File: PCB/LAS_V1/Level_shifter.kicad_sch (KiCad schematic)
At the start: 6 parts, among them Q4 AO3400A, Q5 AO3400A

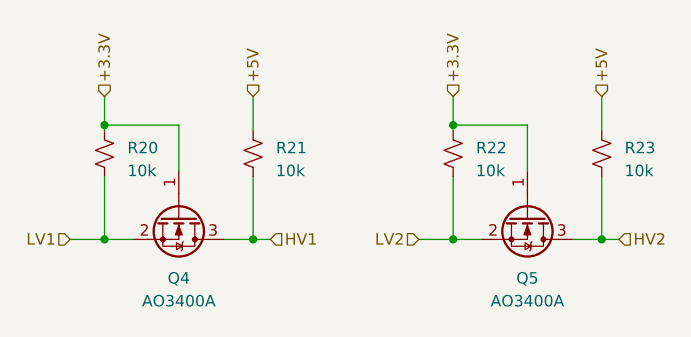
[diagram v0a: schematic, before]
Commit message: added JLBPCB part Numbers
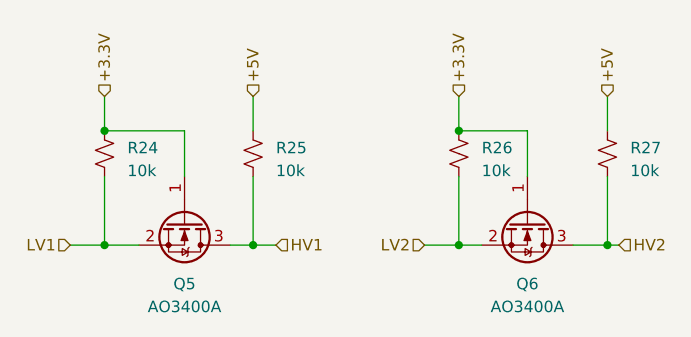
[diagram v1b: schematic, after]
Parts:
- Q5: renamed from Q4; LCSC (none) -> C20917
- Q6: renamed from Q5; LCSC (none) -> C20917
- R24: renamed from R20; footprint (none) -> Resistor_SMD:R_1206_3216Metric; LCSC (none) -> C17902
- R25: renamed from R21; footprint (none) -> Resistor_SMD:R_1206_3216Metric; LCSC (none) -> C17902
- R26: renamed from R22; footprint (none) -> Resistor_SMD:R_1206_3216Metric; LCSC (none) -> C17902
- R27: renamed from R23; footprint (none) -> Resistor_SMD:R_1206_3216Metric; LCSC (none) -> C17902
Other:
- moved on the sheet: Q5, Q6, R26, R27

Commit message: All components Placed on PCB
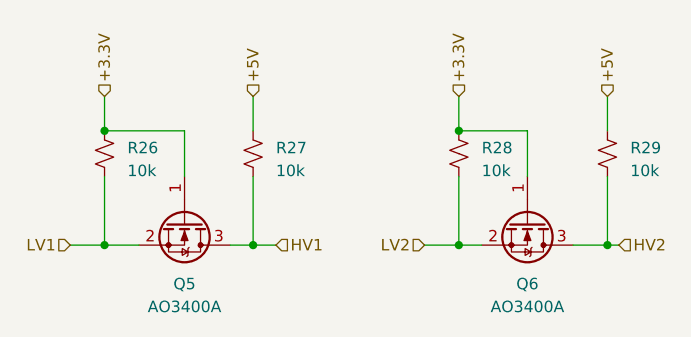
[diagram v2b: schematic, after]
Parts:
- renumbered R24 to R26, R25 to R27, R26 to R28, R27 to R29
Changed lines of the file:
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@@
   (symbol (lib_id "Device:R_Small_US") (at 105.41 77.47 0) (unit 1)
     (in_bom yes) (on_board yes) (dnp no) (fields_autoplaced)
-    (property "Reference" "R24" (at 107.95 76.835 0)
+    (property "Reference" "R26" (at 107.95 76.835 0)
       (effects (font (size 1.27 1.27)) (justify left))
     )
@@
       (project "LAS_V1"
         (path "/aadef4b8-3115-4a49-998f-828f2021a6b4/ed9f2215-51a0-424e-affe-14c415341265"
-          (reference "R24") (unit 1)
+          (reference "R26") (unit 1)
         )
       )
@@
   (symbol (lib_id "Device:R_Small_US") (at 161.29 77.47 0) (unit 1)
     (in_bom yes) (on_board yes) (dnp no) (fields_autoplaced)
-    (property "Reference" "R27" (at 163.83 76.835 0)
+    (property "Reference" "R29" (at 163.83 76.835 0)
       (effects (font (size 1.27 1.27)) (justify left))
     )
@@
       (project "LAS_V1"
         (path "/aadef4b8-3115-4a49-998f-828f2021a6b4/ed9f2215-51a0-424e-affe-14c415341265"
-          (reference "R27") (unit 1)
+          (reference "R29") (unit 1)
         )
       )
@@
   (symbol (lib_id "Device:R_Small_US") (at 144.78 77.47 0) (unit 1)
     (in_bom yes) (on_board yes) (dnp no) (fields_autoplaced)
-    (property "Reference" "R26" (at 147.32 76.835 0)
+    (property "Reference" "R28" (at 147.32 76.835 0)
       (effects (font (size 1.27 1.27)) (justify left))
     )
@@
       (project "LAS_V1"
         (path "/aadef4b8-3115-4a49-998f-828f2021a6b4/ed9f2215-51a0-424e-affe-14c415341265"
-          (reference "R26") (unit 1)
+          (reference "R28") (unit 1)
         )
       )
@@
   (symbol (lib_id "Device:R_Small_US") (at 121.92 77.47 0) (unit 1)
     (in_bom yes) (on_board yes) (dnp no) (fields_autoplaced)
-    (property "Reference" "R25" (at 124.46 76.835 0)
+    (property "Reference" "R27" (at 124.46 76.835 0)
       (effects (font (size 1.27 1.27)) (justify left))
     )
@@
       (project "LAS_V1"
         (path "/aadef4b8-3115-4a49-998f-828f2021a6b4/ed9f2215-51a0-424e-affe-14c415341265"
-          (reference "R25") (unit 1)
+          (reference "R27") (unit 1)
         )
       )
